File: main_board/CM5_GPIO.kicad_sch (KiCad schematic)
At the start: 32 parts, among them IC4 TS921ID, IC6 TS921ID, J8 AudioJack3

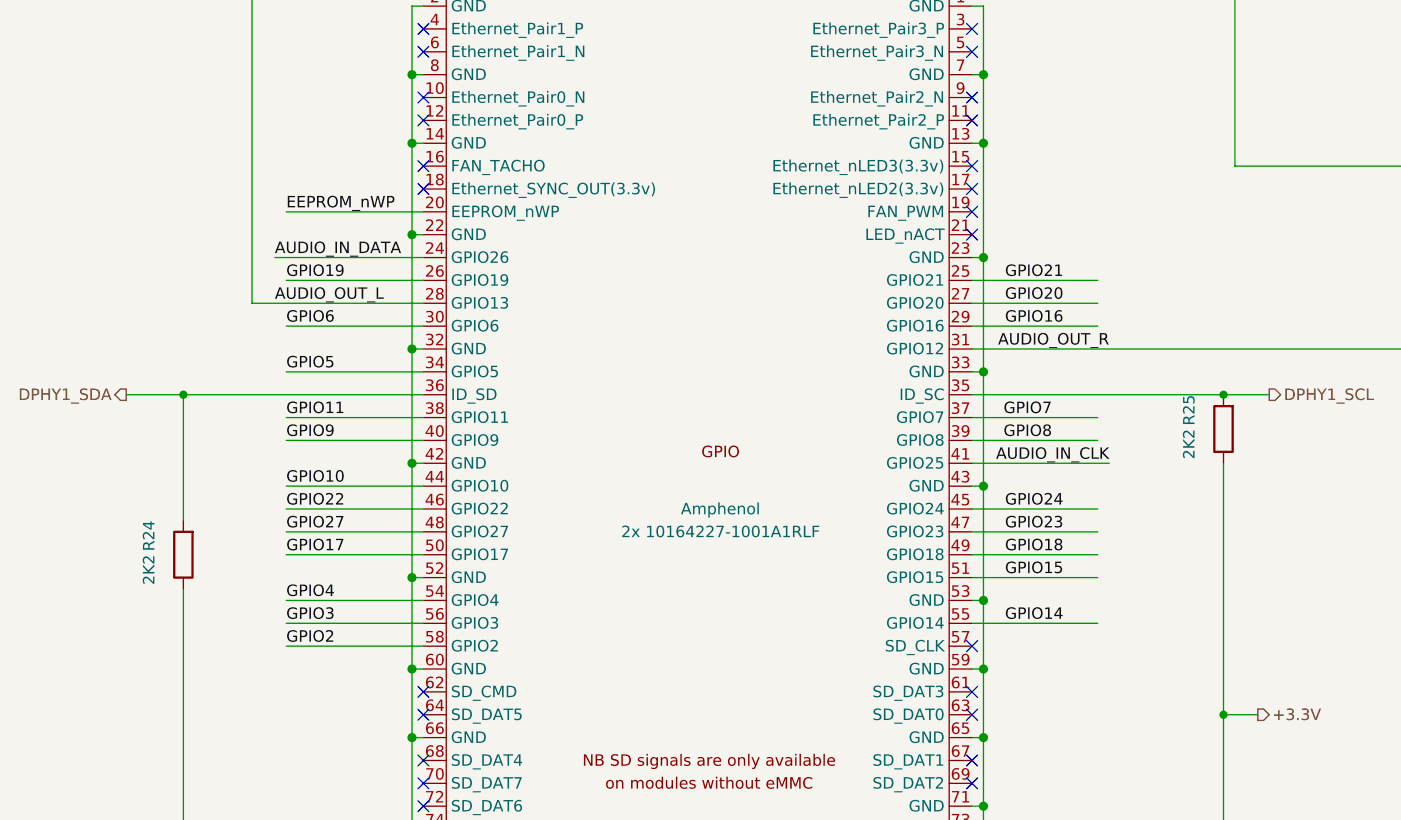
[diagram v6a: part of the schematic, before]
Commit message: Add expansion slot
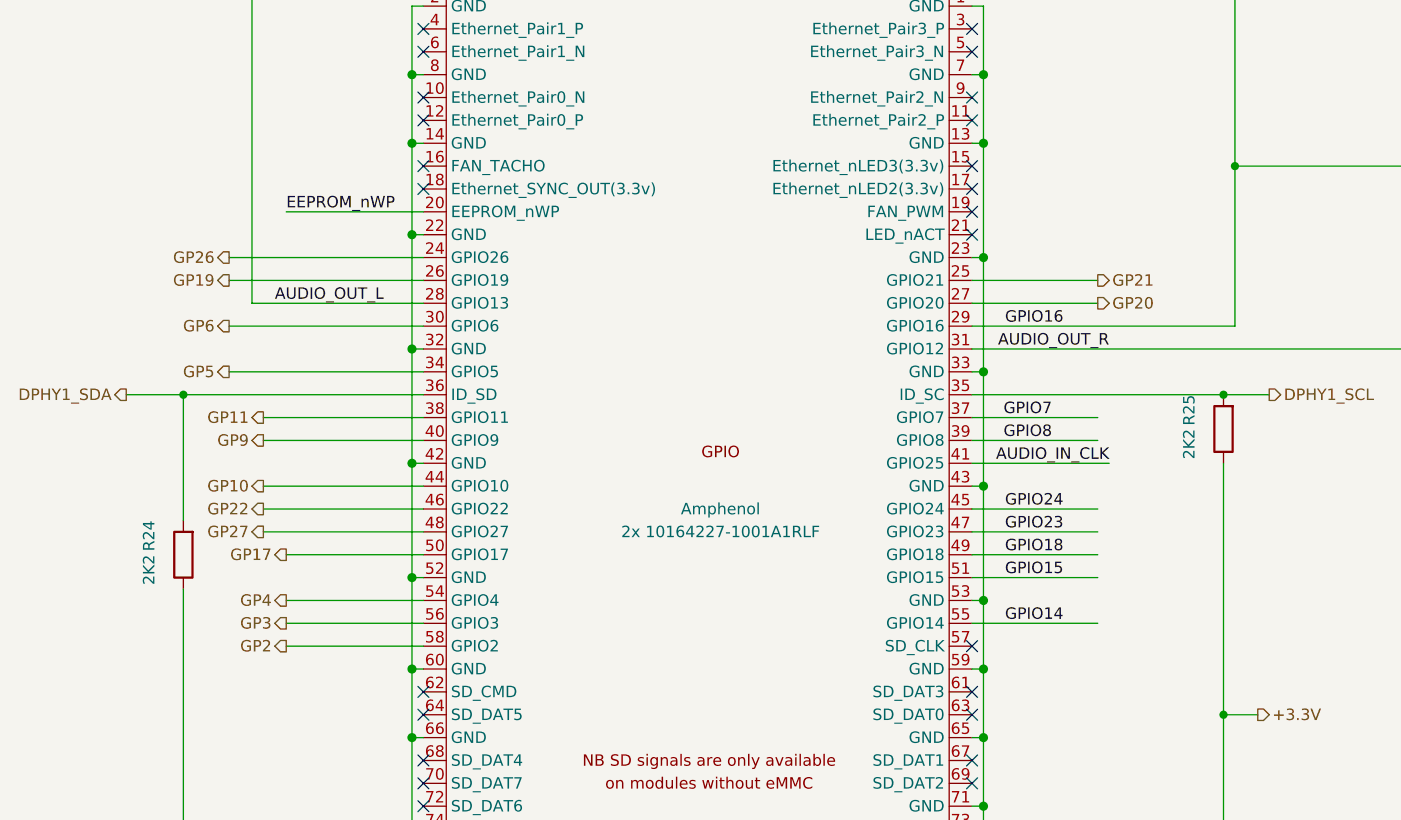
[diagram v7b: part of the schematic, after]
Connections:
- net GPIO16 is gone; now on net AUDIO_OUT_L: Module1.29 (GPIO16)
- net AUDIO_IN_DATA renamed GP26
- net GPIO10 renamed GP10
- net GPIO11 renamed GP11
- net GPIO17 renamed GP17
- net GPIO19 renamed GP19
- net GPIO2 renamed GP2
- net GPIO20 renamed GP20
- net GPIO21 renamed GP21
- net GPIO22 renamed GP22
- net GPIO27 renamed GP27
- net GPIO3 renamed GP3
- net GPIO4 renamed GP4
- net GPIO5 renamed GP5
- net GPIO6 renamed GP6
- net GPIO9 renamed GP9

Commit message: Make sure, that audio jack can be hand soldered, finalize rev 1 design.
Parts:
- J8: footprint Connector_Audio:Jack_3.5mm_CUI_SJ1-3523N_Horizontal -> 000_custom:LUMBERG 1503 16; symbol Connector_Audio:AudioJack3 -> Connector_Audio:AudioJack4
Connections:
- net GND: now also J8.R2
- net at C61.1: now also J8.T; no longer J8.R
- net at C57.1: now also J8.R1; no longer J8.T
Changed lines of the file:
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@@
 	)
 	(junction
+		(at 262.89 119.38)
+		(diameter 0)
+		(color 0 0 0 0)
+	)
+	(junction
 		(at 196.85 15.24)
 		(diameter 0)
@@
 	(wire
 		(pts
+			(xy 274.32 127) (xy 262.89 127)
+		)
+		(stroke
+			(width 0)
+			(type default)
+		)
+	)
+	(wire
+		(pts
 			(xy 209.55 67.31) (xy 275.59 67.31)
 		)
@@
 	(wire
 		(pts
-			(xy 274.32 121.92) (xy 274.32 106.68)
+			(xy 274.32 106.68) (xy 274.32 127)
 		)
 		(stroke
@@
 	(wire
 		(pts
-			(xy 262.89 121.92) (xy 274.32 121.92)
-		)
-		(stroke
-			(width 0)
-			(type default)
-		)
-	)
-	(wire
-		(pts
 			(xy 265.43 119.38) (xy 265.43 129.54)
 		)
@@
 	(wire
 		(pts
-			(xy 262.89 124.46) (xy 279.4 124.46)
-		)
-		(stroke
-			(width 0)
-			(type default)
-		)
-	)
-	(wire
-		(pts
 			(xy 210.82 15.24) (xy 275.59 15.24)
 		)
@@
 	(wire
 		(pts
+			(xy 262.89 119.38) (xy 262.89 121.92)
+		)
+		(stroke
+			(width 0)
+			(type default)
+		)
+	)
+	(wire
+		(pts
 			(xy 121.92 60.96) (xy 135.89 60.96)
 		)
@@
 	(wire
 		(pts
-			(xy 279.4 124.46) (xy 279.4 54.61)
-		)
-		(stroke
-			(width 0)
-			(type default)
-		)
-	)
-	(wire
-		(pts
 			(xy 151.13 66.04) (xy 151.13 48.26)
 		)
@@
 	(wire
 		(pts
+			(xy 262.89 124.46) (xy 279.4 124.46)
+		)
+		(stroke
+			(width 0)
+			(type default)
+		)
+	)
+	(wire
+		(pts
 			(xy 121.92 134.62) (xy 121.92 137.16)
 		)
@@
 		)
 	)
+	(wire
+		(pts
+			(xy 279.4 124.46) (xy 279.4 54.61)
+		)
+		(stroke
+			(width 0)
+			(type default)
+		)
+	)
 	(label "AUDIO_IN_CLK"
 		(at 137.16 81.28 180)
@@
 	)
 	(symbol
-		(lib_id "Connector_Audio:AudioJack3")
+		(lib_id "Connector_Audio:AudioJack4")
 		(at 257.81 121.92 0)
 		(unit 1)
@@
 		(fields_autoplaced yes)
 		(property "Reference" "J8"
-			(at 255.905 113.03 0)
+			(at 255.27 113.03 0)
 			(effects
 				(font
@@
 		)
 		(property "Value" "AudioJack3"
-			(at 255.905 115.57 0)
+			(at 255.27 115.57 0)
 			(effects
 				(font
@@
 			)
 		)
-		(property "Footprint" "Connector_Audio:Jack_3.5mm_CUI_SJ1-3523N_Horizontal"
+		(property "Footprint" "000_custom:LUMBERG 1503 16"
 			(at 257.81 121.92 0)
 			(effects
@@
 			)
 		)
-		(property "Description" "Audio Jack, 3 Poles (Stereo / TRS)"
+		(property "Description" "Audio Jack, 4 Poles (TRRS)"
 			(at 257.81 121.92 0)
 			(effects
@@
 		(pin "S"
 		)
-		(pin "R"
+		(pin "R1"
 		)
 		(pin "T"
 		)
+		(pin "R2"
+		)
 		(instances
